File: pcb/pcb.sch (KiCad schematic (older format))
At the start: 18 parts, among them J1 BAT+, J2 BAT-, J3 Molex, SW1 Reset, SW2 Flash, U1 BOB-13263, U2 ESP-12F, U3 TP4056, U4 GY-521, U5 VREG

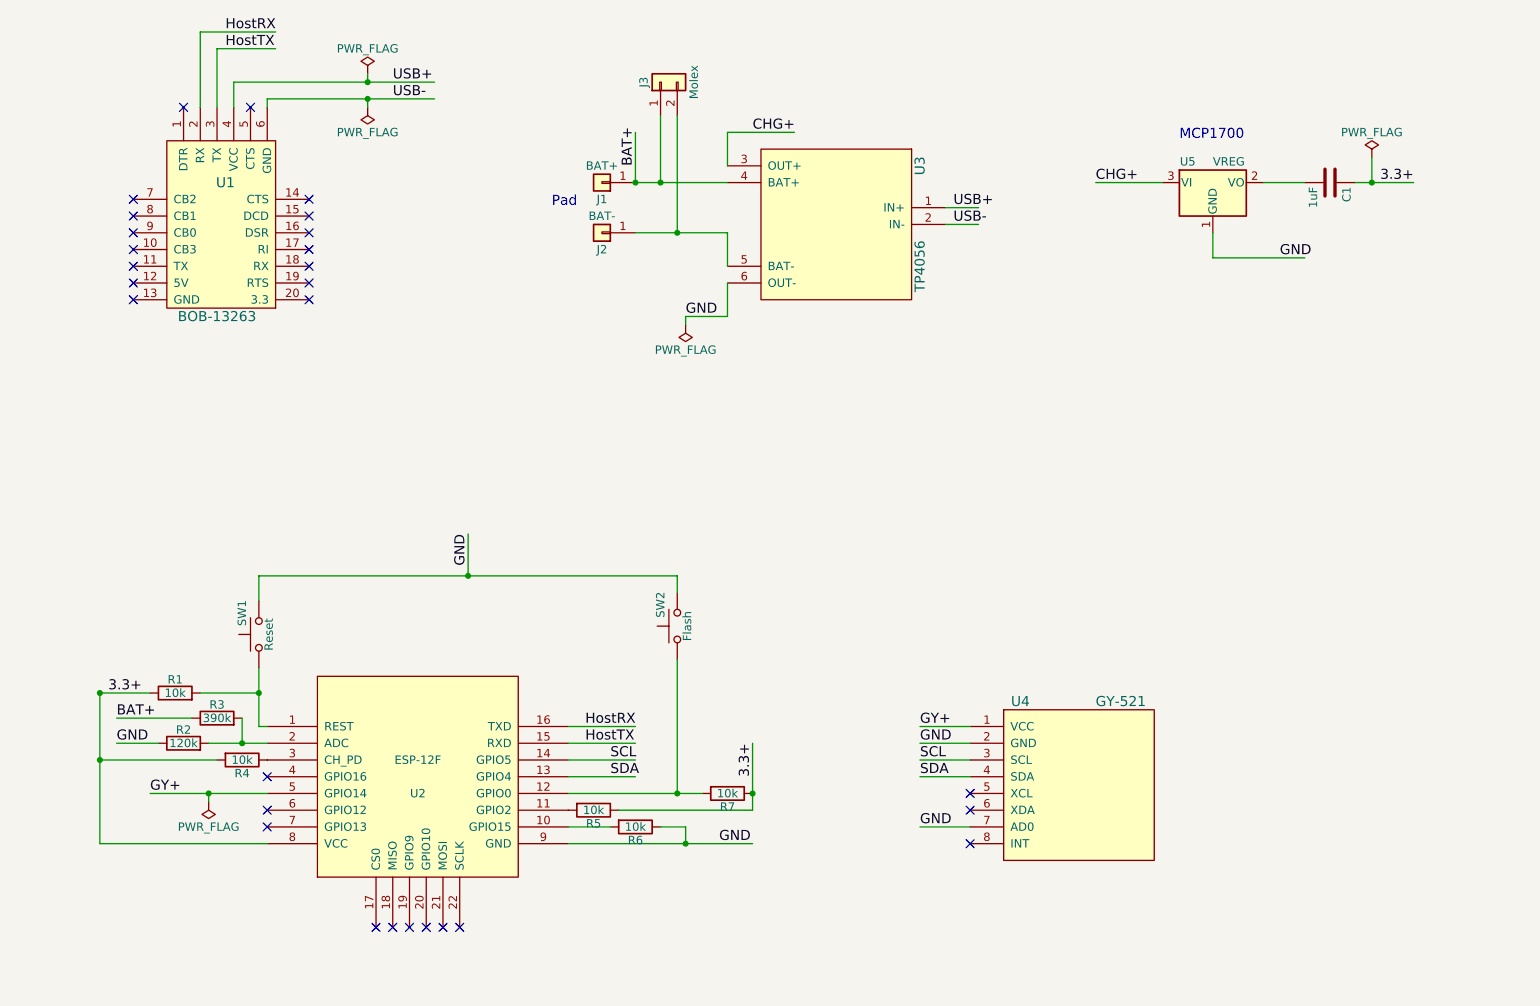
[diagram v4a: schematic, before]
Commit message: Fix problems from Capacitors 101
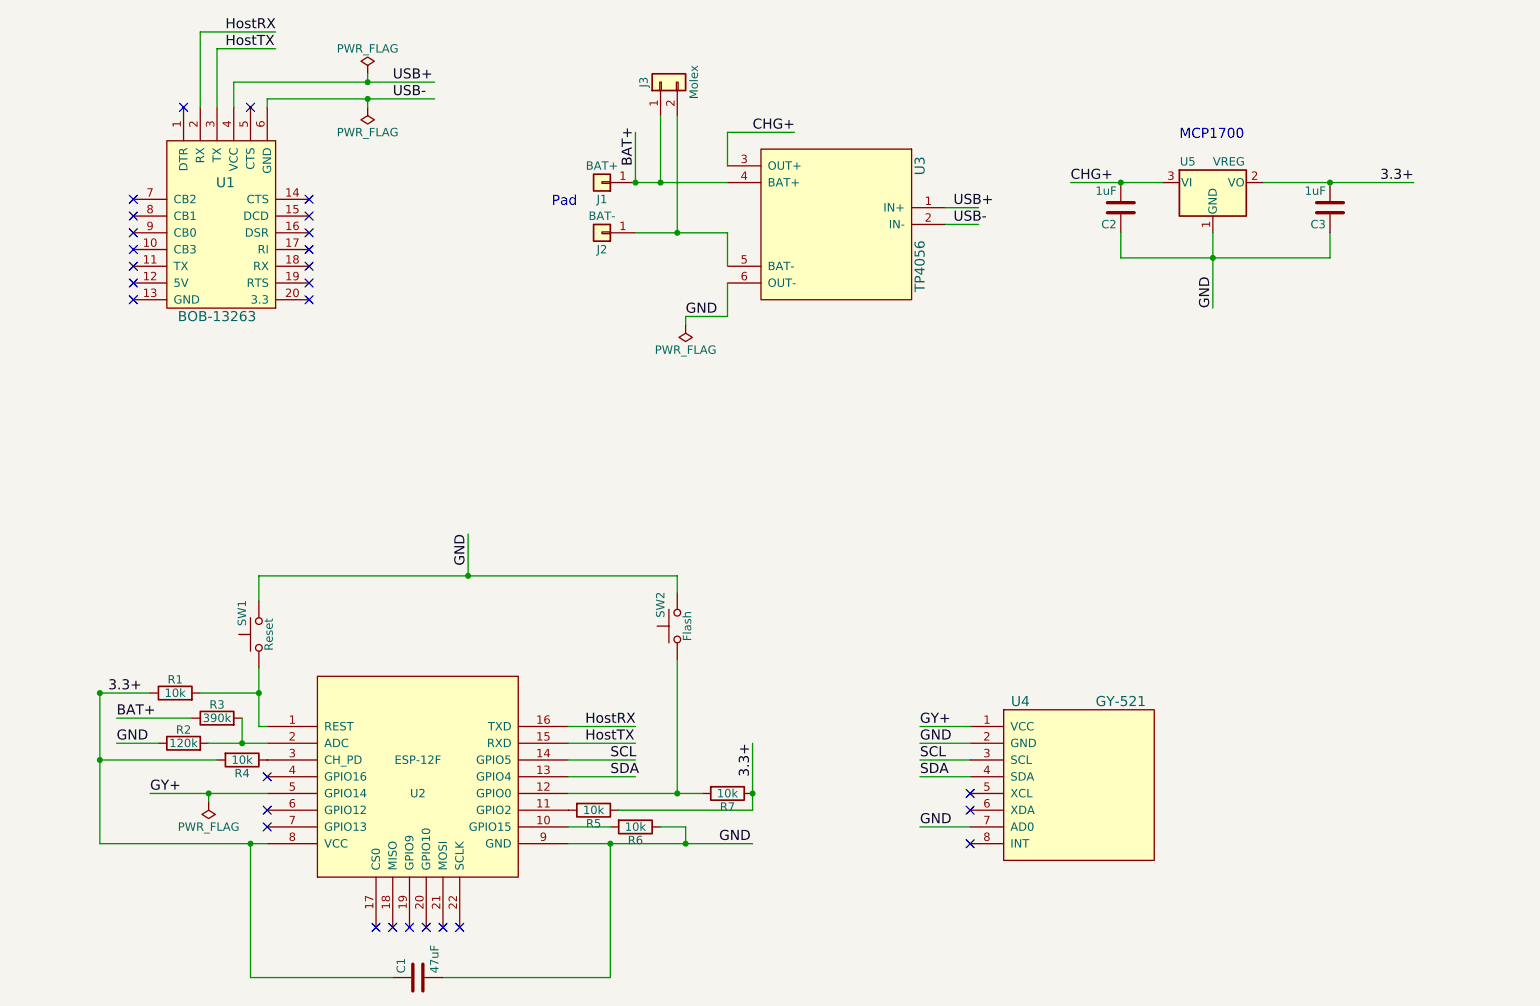
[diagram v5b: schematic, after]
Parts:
- added C1: 47uF, Capacitors_SMD:C_1206_HandSoldering, symbol C
- added C2: 1uF, Capacitors_SMD:C_1206_HandSoldering, symbol C
- renumbered C1 to C3
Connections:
- wire segments 63 -> 67
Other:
- moved on the sheet: C3
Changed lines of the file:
@@
 Text Label 6100 1950 0    60   ~ 0
 CHG+
-Text Label 8150 2250 0    60   ~ 0
+Text Label 8000 2250 0    60   ~ 0
 CHG+
 Text Label 9850 2250 0    60   ~ 0
 3.3+
-Text Label 9250 2700 0    60   ~ 0
+Text Label 8850 3000 1    60   ~ 0
 GND
 Text Label 5400 2150 1    60   ~ 0
@@
 NoConn ~ 3200 6100
 $Comp
-L C C1
+L C C3
 U 1 1 5B2296F3
-P 9550 2250
-F 0 "C1" H 9575 2350 50  0000 L CNN
-F 1 "1uF" H 9575 2150 50  0000 L CNN
-F 2 "Capacitors_SMD:C_1206_HandSoldering" H 9588 2100 50  0001 C CNN
-F 3 "" H 9550 2250 50  0001 C CNN
-	1    9550 2250
-	0    1    1    0
-$EndComp
-$Comp
-L PWR_FLAG #FLG03
-U 1 1 5B22C3B3
-P 9800 2100
-F 0 "#FLG03" H 9800 2175 50  0001 C CNN
-F 1 "PWR_FLAG" H 9800 2250 50  0000 C CNN
-F 2 "" H 9800 2100 50  0001 C CNN
-F 3 "" H 9800 2100 50  0001 C CNN
-	1    9800 2100
-	1    0    0    -1
+P 9550 2400
+F 0 "C3" H 9575 2500 50  0000 L CNN
+F 1 "1uF" H 9575 2300 50  0000 L CNN
+F 2 "Capacitors_SMD:C_1206_HandSoldering" H 9588 2250 50  0001 C CNN
+F 3 "" H 9550 2400 50  0001 C CNN
+	1    9550 2400
+	-1   0    0    1
 $EndComp
 $Comp
@@
 $EndComp
 $Comp
-L PWR_FLAG #FLG04
+L PWR_FLAG #FLG03
 U 1 1 5B22D046
 P 2850 5950
-F 0 "#FLG04" H 2850 6025 50  0001 C CNN
+F 0 "#FLG03" H 2850 6025 50  0001 C CNN
 F 1 "PWR_FLAG" H 2850 6100 50  0000 C CNN
 F 2 "" H 2850 5950 50  0001 C CNN
@@
 NoConn ~ 2400 2350
 $Comp
-L PWR_FLAG #FLG05
+L PWR_FLAG #FLG04
 U 1 1 5B2225EE
 P 5700 3100
-F 0 "#FLG05" H 5700 3175 50  0001 C CNN
+F 0 "#FLG04" H 5700 3175 50  0001 C CNN
 F 1 "PWR_FLAG" H 5700 3250 50  0000 C CNN
 F 2 "" H 5700 3100 50  0001 C CNN
@@
 	-1   0    0    1
 $EndComp
-Wire Wire Line
-	3000 1650 4200 1650
-Wire Wire Line
-	3000 1650 3000 1800
-Connection ~ 3800 1650
-Wire Wire Line
-	7450 2400 7250 2400
-Wire Wire Line
-	7450 2500 7250 2500
-Wire Wire Line
-	5950 2850 5950 3050
-Wire Wire Line
-	5950 3050 5700 3050
-Wire Wire Line
-	5950 2150 5950 1950
-Wire Wire Line
-	5950 1950 6350 1950
-Wire Wire Line
-	8150 2250 8550 2250
-Wire Wire Line
-	8850 2550 8850 2700
-Wire Wire Line
-	8850 2700 9400 2700
-Wire Wire Line
-	9150 2250 9400 2250
-Wire Wire Line
-	5400 2250 5950 2250
-Wire Wire Line
-	5000 5500 5400 5500
-Wire Wire Line
-	5000 5600 5400 5600
-Wire Wire Line
-	5000 5700 5400 5700
-Wire Wire Line
-	5000 5800 5400 5800
-Wire Wire Line
-	2200 6200 3200 6200
-Wire Wire Line
-	5000 6200 6100 6200
-Wire Wire Line
-	7100 5500 7400 5500
-Wire Wire Line
-	7100 5600 7400 5600
-Wire Wire Line
-	7100 5700 7400 5700
-Wire Wire Line
-	7100 5800 7400 5800
-Wire Wire Line
-	7100 6100 7400 6100
-Wire Wire Line
-	6100 6000 5300 6000
-Wire Wire Line
-	3150 5150 3150 5500
-Wire Wire Line
-	2800 5300 3150 5300
-Wire Wire Line
-	2200 5300 2500 5300
-Wire Wire Line
-	3150 4750 3150 4600
-Connection ~ 3150 5300
-Wire Wire Line
-	2200 5700 2900 5700
-Wire Wire Line
-	2200 5300 2200 6200
-Connection ~ 2200 5300
-Wire Wire Line
-	2500 5900 3200 5900
-Wire Wire Line
-	5000 5900 5800 5900
-Wire Wire Line
-	5650 5100 5650 5900
-Connection ~ 5650 5900
-Wire Wire Line
-	5650 4600 5650 4700
-Wire Wire Line
-	3150 4600 5650 4600
-Wire Wire Line
-	4400 4600 4400 4350
-Connection ~ 4400 4600
-Connection ~ 2200 5700
-Wire Wire Line
-	6100 5600 6100 6000
-Connection ~ 6100 5900
-Wire Wire Line
-	5000 6100 5250 6100
-Wire Wire Line
-	5550 6100 5700 6100
-Wire Wire Line
-	5700 6100 5700 6200
-Connection ~ 5700 6200
-Wire Wire Line
-	3150 5500 3200 5500
-Wire Wire Line
-	9700 2250 10050 2250
-Wire Wire Line
-	9800 2100 9800 2250
-Connection ~ 9800 2250
-Wire Wire Line
-	2850 5950 2850 5900
-Connection ~ 2850 5900
-Wire Wire Line
-	5400 2250 5400 1950
-Connection ~ 5400 2250
-Wire Wire Line
-	3200 1800 3200 1750
-Wire Wire Line
-	3200 1750 4200 1750
-Wire Wire Line
-	3800 1600 3800 1650
-Wire Wire Line
-	3800 1800 3800 1750
-Connection ~ 3800 1750
-Wire Wire Line
-	2800 1800 2800 1350
-Wire Wire Line
-	2800 1350 3250 1350
-Wire Wire Line
-	2900 1450 2900 1800
-Wire Wire Line
-	2900 1450 3250 1450
-Wire Wire Line
-	5400 2550 5950 2550
-Wire Wire Line
-	5950 2550 5950 2750
-Wire Wire Line
-	5700 3050 5700 3100
-Wire Wire Line
-	5550 1850 5550 2250
-Connection ~ 5550 2250
 Text Notes 4900 2400 0    60   ~ 0
 Pad
@@
 	0    -1   -1   0
 $EndComp
-Wire Wire Line
-	5650 1850 5650 2550
-Connection ~ 5650 2550
 Text Notes 8650 2000 0    60   ~ 0
 MCP1700
@@
 	0    -1   -1   0
 $EndComp
+Text Label 2300 5600 0    60   ~ 0
+GND
+$Comp
+L C C2
+U 1 1 5B241212
+P 8300 2400
+F 0 "C2" H 8325 2500 50  0000 L CNN
+F 1 "1uF" H 8325 2300 50  0000 L CNN
+F 2 "Capacitors_SMD:C_1206_HandSoldering" H 8338 2250 50  0001 C CNN
+F 3 "" H 8300 2400 50  0001 C CNN
+	1    8300 2400
+	-1   0    0    1
+$EndComp
+Wire Wire Line
+	3000 1650 4200 1650
+Wire Wire Line
+	3000 1650 3000 1800
+Connection ~ 3800 1650
+Wire Wire Line
+	7450 2400 7250 2400
+Wire Wire Line
+	7450 2500 7250 2500
+Wire Wire Line
+	5950 2850 5950 3050
+Wire Wire Line
+	5950 3050 5700 3050
+Wire Wire Line
+	5950 2150 5950 1950
+Wire Wire Line
+	5950 1950 6350 1950
+Wire Wire Line
+	8000 2250 8550 2250
+Wire Wire Line
+	8850 2550 8850 3000
+Wire Wire Line
+	9150 2250 10050 2250
+Wire Wire Line
+	5400 2250 5950 2250
+Wire Wire Line
+	5000 5500 5400 5500
+Wire Wire Line
+	5000 5600 5400 5600
+Wire Wire Line
+	5000 5700 5400 5700
+Wire Wire Line
+	5000 5800 5400 5800
+Wire Wire Line
+	2200 6200 3200 6200
+Wire Wire Line
+	5000 6200 6100 6200
+Wire Wire Line
+	7100 5500 7400 5500
+Wire Wire Line
+	7100 5600 7400 5600
+Wire Wire Line
+	7100 5700 7400 5700
+Wire Wire Line
+	7100 5800 7400 5800
+Wire Wire Line
+	7100 6100 7400 6100
+Wire Wire Line
+	6100 6000 5300 6000
+Wire Wire Line
+	3150 5150 3150 5500
+Wire Wire Line
+	2800 5300 3150 5300
+Wire Wire Line
+	2200 5300 2500 5300
+Wire Wire Line
+	3150 4750 3150 4600
+Connection ~ 3150 5300
+Wire Wire Line
+	2200 5700 2900 5700
+Wire Wire Line
+	2200 5300 2200 6200
+Connection ~ 2200 5300
+Wire Wire Line
+	2500 5900 3200 5900
+Wire Wire Line
+	5000 5900 5800 5900
+Wire Wire Line
+	5650 5100 5650 5900
+Connection ~ 5650 5900
+Wire Wire Line
+	5650 4600 5650 4700
+Wire Wire Line
+	3150 4600 5650 4600
+Wire Wire Line
+	4400 4600 4400 4350
+Connection ~ 4400 4600
+Connection ~ 2200 5700
+Wire Wire Line
+	6100 5600 6100 6000
+Connection ~ 6100 5900
+Wire Wire Line
+	5000 6100 5250 6100
+Wire Wire Line
+	5550 6100 5700 6100
+Wire Wire Line
+	3150 5500 3200 5500
+Wire Wire Line
+	2850 5950 2850 5900
+Connection ~ 2850 5900
+Wire Wire Line
+	5400 2250 5400 1950
+Connection ~ 5400 2250
+Wire Wire Line
+	3200 1800 3200 1750
+Wire Wire Line
+	3200 1750 4200 1750
+Wire Wire Line
+	3800 1600 3800 1650
+Wire Wire Line
+	3800 1800 3800 1750
+Connection ~ 3800 1750
+Wire Wire Line
+	2800 1800 2800 1350
+Wire Wire Line
+	2800 1350 3250 1350
+Wire Wire Line
+	2900 1450 2900 1800
+Wire Wire Line
+	2900 1450 3250 1450
+Wire Wire Line
+	5400 2550 5950 2550
+Wire Wire Line
+	5950 2550 5950 2750
+Wire Wire Line
+	5700 3050 5700 3100
+Wire Wire Line
+	5550 1850 5550 2250
+Connection ~ 5550 2250
+Wire Wire Line
+	5650 1850 5650 2550
+Connection ~ 5650 2550
 Wire Wire Line
 	2300 5450 2750 5450
@@
 Wire Wire Line
 	2550 5600 2300 5600
-Text Label 2300 5600 0    60   ~ 0
-GND
+Wire Wire Line
+	3100 6200 3100 7000
+Wire Wire Line
+	3100 7000 3950 7000
+Connection ~ 3100 6200
+Wire Wire Line
+	5250 7000 4250 7000
+Wire Wire Line
+	9550 2700 9550 2550
+Wire Wire Line
+	8300 2700 9550 2700
+Connection ~ 9550 2250
+Connection ~ 8300 2250
+Wire Wire Line
+	8300 2550 8300 2700
+Wire Wire Line
+	5250 7000 5250 6200
+Connection ~ 5250 6200
+Wire Wire Line
+	5700 6100 5700 6200
+Connection ~ 5700 6200
+Connection ~ 8850 2700
+$Comp
+L C C1
+U 1 1 5B2439F8
+P 4100 7000
+F 0 "C1" H 4125 7100 50  0000 L CNN
+F 1 "47uF" H 4125 6900 50  0000 L CNN
+F 2 "Capacitors_SMD:C_1206_HandSoldering" H 4138 6850 50  0001 C CNN
+F 3 "" H 4100 7000 50  0001 C CNN
+	1    4100 7000
+	0    -1   -1   0
+$EndComp
 $EndSCHEMATC
